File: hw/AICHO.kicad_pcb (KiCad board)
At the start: 2 copper layers, 100 x 58 mm, 77 parts, among them J1 Conn_01x06, J101 Conn_01x03, J102 Conn_01x02, J103 Conn_01x02, J104 Conn_01x02, J201 Conn_01x03, J202 Conn_01x02, J203 Conn_01x02, J204 Conn_01x02, J21 Conn_01x02, J22 Conn_01x02, J3 USB_A, J301 Conn_01x03, J302 Conn_01x02, J303 Conn_01x02, J304 Conn_01x02, J4 AudioJack3_SwitchTR, J401 Conn_01x03, J402 Conn_01x02, J403 Conn_01x02, J404 Conn_01x02, J5 Speaker, Q1 Si2302, Q10 Si2302, Q11 Si2302, Q12 Si2302, Q2 Si2302, Q3 Si2302, Q4 Si2302, Q5 Si2302, Q6 Si2302, Q7 Si2302, Q8 Si2302, Q9 Si2302, U1 RP2040, U2 W25Q128JVPIQ, U3 SPX3819M5-L-3-3, U4 USBLC6-2SC6, U5 MAX98357AETE+, Y1 12MHz

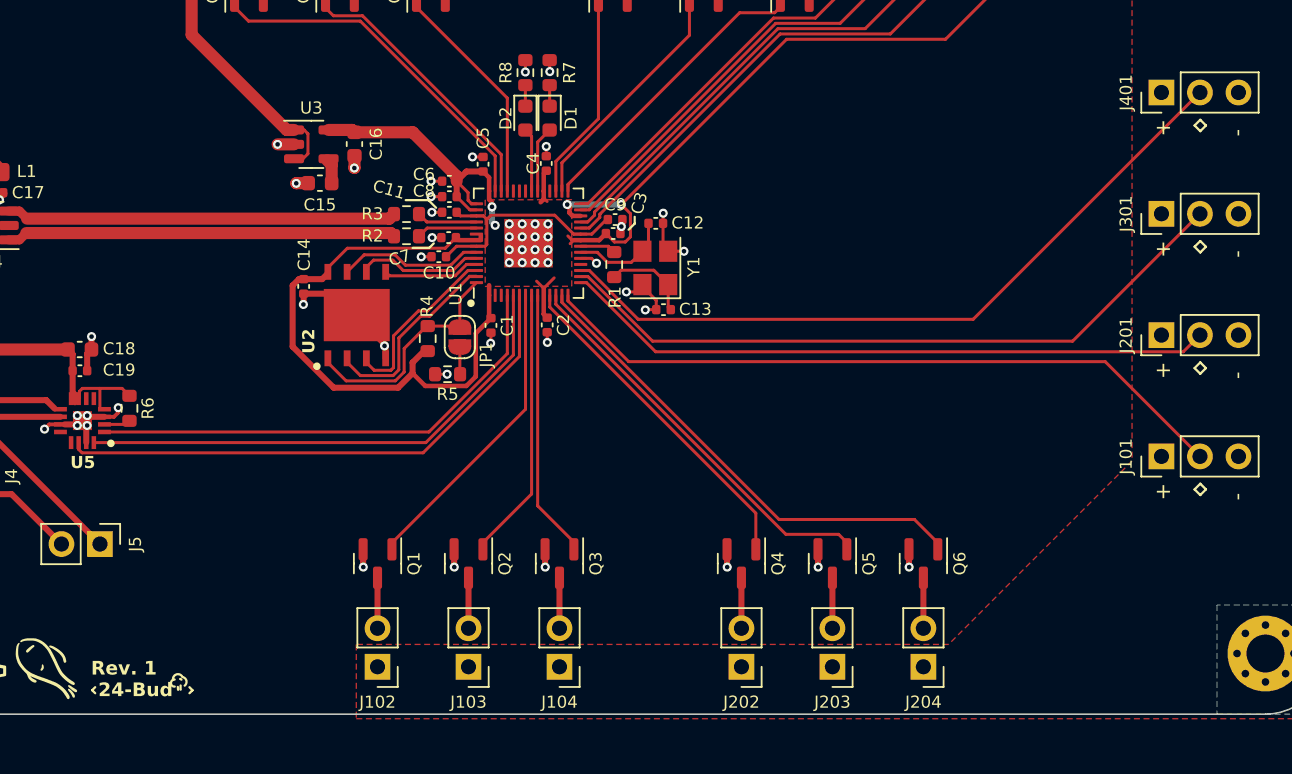
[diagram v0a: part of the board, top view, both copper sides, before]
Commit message: Fix missing level shifter and resubmit for fab >-<
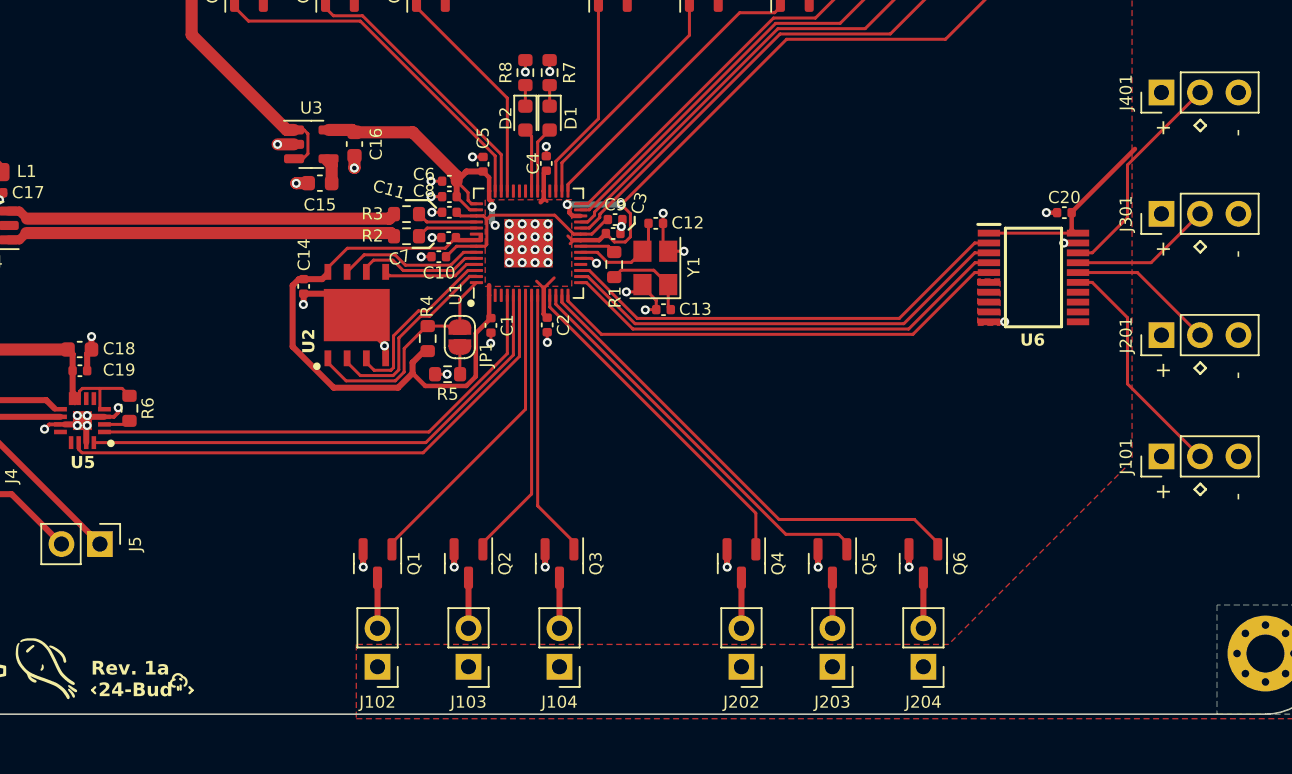
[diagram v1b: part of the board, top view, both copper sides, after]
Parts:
- added C20: 100n, Capacitor_SMD:C_0402_1005Metric, F.Cu at (112.7, 54.9)
- added U6: SN74AHCT245PWR, SN74AHCT245PWR:SOP65P640X120-20N, F.Cu at (110.7, 59.2)
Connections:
- J101 pad 2: /ORG1_LED -> /ORG1_LED_OUT
- J201 pad 2: /ORG2_LED -> /ORG2_LED_OUT
- J301 pad 2: /ORG3_LED -> /ORG3_LED_OUT
- J401 pad 2: /ORG4_LED -> /ORG4_LED_OUT
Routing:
- net /ORG4_LED: track 48.4 -> 30.3 mm
- net /ORG3_LED: track 46.1 -> 30.1 mm
- net /ORG1_LED: track 46.3 -> 30.7 mm
- net /ORG1_LED_OUT: track 0.00 -> 15.4 mm
- net /ORG4_LED_OUT: track 0.00 -> 14.5 mm
- net +5V: track 96.3 -> 109.8 mm
- net /ORG2_LED: track 43.2 -> 30.0 mm
- net /ORG2_LED_OUT: track 0.00 -> 9.75 mm
- net /ORG3_LED_OUT: track 0.00 -> 9.38 mm
- net GND: track 54.7 -> 57.4 mm, vias 62 -> 65
- added copper zone on F.Cu, net GND
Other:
- board text added: "Rev. 1a"
- board text removed: "Rev. 1"

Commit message: 🚧 Update layout
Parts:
- removed the R6 at (51.1, 67.8)
- added C20: 10u, Capacitor_SMD:C_0603_1608Metric, F.Cu at (57.3, 75.4)
- added C21: 100n, Capacitor_SMD:C_0402_1005Metric, F.Cu at (58.5, 74.8)
- added C22: 10u, Capacitor_SMD:C_0603_1608Metric, F.Cu at (57.2, 69.3)
- added C23: 100n, Capacitor_SMD:C_0402_1005Metric, F.Cu at (58.4, 69.9)
- added C24: 10u, Capacitor_SMD:C_0603_1608Metric, F.Cu at (69.9, 70.2)
- added C25: 100n, Capacitor_SMD:C_0402_1005Metric, F.Cu at (68.5, 70.4)
- added C26: 2.2u, Capacitor_SMD:C_0402_1005Metric, F.Cu at (61.7, 68.2)
- added C27: 2.2u, Capacitor_SMD:C_0402_1005Metric, F.Cu at (58.0, 71.5)
- added C28: 2.2n, Capacitor_SMD:C_0402_1005Metric, F.Cu at (56.0, 72.0)
- added C29: 2.2n, Capacitor_SMD:C_0402_1005Metric, F.Cu at (56.0, 73.8)
- added C30: 100n, Capacitor_SMD:C_0402_1005Metric, F.Cu at (54.5, 73.0)
- added C31: 1u, Capacitor_SMD:C_0402_1005Metric, F.Cu at (2.07, 97.9)
- added C32: 2.2u, Capacitor_SMD:C_0402_1005Metric, F.Cu at (2.07, 96.9)
- added C33: 470n, Capacitor_SMD:C_0402_1005Metric, F.Cu at (8.18, 97.3)
- added C34: 470n, Capacitor_SMD:C_0402_1005Metric, F.Cu at (4.04, 95.2)
- added C35: 100n, Capacitor_SMD:C_0402_1005Metric, F.Cu at (8.18, 98.8)
- added C36: 10u, Capacitor_SMD:C_0603_1608Metric, F.Cu at (-10.8, 101.1)
- added C37: 100n, Capacitor_SMD:C_0402_1005Metric, F.Cu at (-9.55, 101.1)
- added C38: 10u, Capacitor_SMD:C_0603_1608Metric, F.Cu at (-10.8, 98.1)
- added C39: 100n, Capacitor_SMD:C_0402_1005Metric, F.Cu at (-9.55, 99.3)
- added C40: 10u, Capacitor_SMD:C_0603_1608Metric, F.Cu at (-8.13, 95.5)
- added C41: 100n, Capacitor_SMD:C_0402_1005Metric, F.Cu at (-8.13, 96.7)
- added C42: 2.2u, Capacitor_SMD:C_0402_1005Metric, F.Cu at (2.05, 98.8)
- added C43: 2.2n, Capacitor_SMD:C_0402_1005Metric, F.Cu at (-0.29, 100.2)
- added J6: AudioJack3_SwitchTR, Connector_Audio:Jack_3.5mm_CUI_SJ1-3525N_Horizontal, F.Cu at (56.0, 93.5)
- added R10: 2.2k, Resistor_SMD:R_0402_1005Metric, F.Cu at (9.58, 98.4)
- added R11: 150k, Resistor_SMD:R_0402_1005Metric, F.Cu at (7.25, 95.2)
- added R12: 100k, Resistor_SMD:R_0402_1005Metric, F.Cu at (8.19, 96.4)
- added R13: 470, Resistor_SMD:R_0402_1005Metric, F.Cu at (0.20, 98.8)
- added R8: 470, Resistor_SMD:R_0402_1005Metric, F.Cu at (58.0, 72.4)
- added R9: 470, Resistor_SMD:R_0402_1005Metric, F.Cu at (58.0, 73.3)
- added U6: OPA1622, Package_SON:Texas_S-PVSON-N10, F.Cu at (51.8, 73.0)
- added U7: MAX9814, Package_DFN_QFN:DFN-14-1EP_3x3mm_P0.4mm_EP1.78x2.35mm, F.Cu at (5.13, 97.5)
- added U8: PCM1808PWR, PCM1808PWR:PCM1808PWR, F.Cu at (-4.95, 100.5)
- U5: value MAX98357AETE+ -> PCM5102A; footprint MAX98357AETE+:QFN50P300X300X80-17N -> Package_SO:TSSOP-20_4.4x6.5mm_P0.65mm
- moved C18 21.1 mm to (68.5, 67.9)
- moved C19 20.2 mm to (67.5, 69.7), turned to -90 degrees
- moved U5 15.3 mm to (62.9, 72.3), turned to 0 degrees
- moved G*** 10.0 mm to (45.7, 95.1)
- moved G*** 10.0 mm to (40.7, 94.9)
- moved H2 10.0 mm to (34.0, 94.0)
- moved H3 10.0 mm to (126.0, 94.0)
- moved J102 10.0 mm to (67.4, 94.9)
- moved J103 10.0 mm to (73.4, 94.9)
- moved J104 10.0 mm to (79.4, 94.9)
- moved J202 10.0 mm to (91.4, 94.9)
- moved J203 10.0 mm to (97.4, 94.9)
- moved J204 10.0 mm to (103.4, 94.9)
- moved J4 10.0 mm to (34.5, 82.3)
- moved Q1 10.0 mm to (67.4, 88.1)
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- renumbered C20 to C45, J3 to J2, R7 to R6, R8 to R7, U6 to U9
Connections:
- C18 pad 1: +5V -> +3V3
- C19 pad 1: +5V -> +3V3
- J4 pad R: /AUDIO_OUT+ -> /AUDIO_OUT_R
- J4 pad RN: /AUDIO_SPEAKER+ -> unconnected-(J4-PadRN)
- J4 pad S: /AUDIO_OUT- -> GND
- J4 pad T: /AUDIO_OUT+ -> /AUDIO_OUT_L
- J4 pad TN: unconnected-(J4-PadTN) -> /AUDIO_SPEAKER+
- J5 pad 2: /AUDIO_OUT- -> GND
- U1 pad 11: /ORG2_SOLENOID -> /MIC_SHDN
- U1 pad 12: /ORG2_PUMP_INFLATE -> unconnected-(U1-GPIO9-Pad12)
- U1 pad 13: /ORG2_PUMP_DRAIN -> /ORG1_SOLENOID
- U1 pad 14: /ORG1_LED -> /ORG1_PUMP_INFLATE
- U1 pad 15: /ORG2_LED -> /ORG1_PUMP_DRAIN
- U1 pad 16: /ORG3_LED -> /ORG2_SOLENOID
- U1 pad 17: /ORG4_LED -> /ORG2_PUMP_INFLATE
- U1 pad 18: unconnected-(U1-GPIO15-Pad18) -> /ORG2_PUMP_DRAIN
- U1 pad 29: /ORG3_SOLENOID -> /ORG1_LED
- U1 pad 3: unconnected-(U1-GPIO1-Pad3) -> /I2S_SD
- U1 pad 30: /ORG3_PUMP_INFLATE -> /ORG2_LED
- U1 pad 31: /ORG3_PUMP_DRAIN -> /ORG3_LED
- U1 pad 32: unconnected-(U1-GPIO21-Pad32) -> /ORG4_LED
- U1 pad 34: /ACT1 -> /ORG3_SOLENOID
- U1 pad 35: /ACT2 -> /ORG3_PUMP_INFLATE
- U1 pad 36: unconnected-(U1-GPIO24-Pad36) -> /ORG3_PUMP_DRAIN
- U1 pad 37: unconnected-(U1-GPIO25-Pad37) -> /ACT1
- U1 pad 38: unconnected-(U1-GPIO26_ADC0-Pad38) -> /ACT2
- U1 pad 4: /I2S_SD -> /I2S_CK
- U1 pad 5: /I2S_CK -> /I2S_WS
- U1 pad 6: /I2S_WS -> /MIC_ADC_SD
- U1 pad 7: /ORG1_SOLENOID -> /MIC_ADC_CK
- U1 pad 8: /ORG1_PUMP_INFLATE -> /MIC_ADC_WS
- U1 pad 9: /ORG1_PUMP_DRAIN -> /MIC_ADC_SCK
- U5 pad 1: /I2S_SD -> +3V3
- U5 pad 10: /AUDIO_OUT- -> GND
- U5 pad 13: unconnected-(U5-N.C._4-Pad13) -> /I2S_CK
- U5 pad 14: /I2S_WS -> /I2S_SD
- U5 pad 15: GND -> /I2S_WS
- U5 pad 16: /I2S_CK -> GND
- U5 pad 17: GND -> +3V3
- U5 pad 4: +5V -> Net-(U5-CAPM)
- U5 pad 5: unconnected-(U5-N.C._1-Pad5) -> Net-(U5-VNEG)
- U5 pad 6: unconnected-(U5-N.C._2-Pad6) -> Net-(U5-OUTL)
- U5 pad 7: +5V -> Net-(U5-OUTR)
- U5 pad 8: +5V -> +3V3
- U5 pad 9: /AUDIO_OUT+ -> GND
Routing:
- net /I2S_CK: track 34.0 -> 3.84 mm
- net /ORG1_LED: track 30.7 -> 0.94 mm
- net /ORG4_LED: track 30.3 -> 0.94 mm
- net /ORG3_LED: track 30.1 -> 0.94 mm
- net /I2S_WS: track 36.3 -> 7.08 mm
- net /ORG2_LED: track 30.0 -> 0.92 mm
- net /AUDIO_OUT-: track 28.1 -> 0.00 mm
- net /I2S_SD: track 32.6 -> 7.99 mm
- net /AUDIO_OUT+: track 24.4 -> 0.00 mm
- net /ORG2_PUMP_INFLATE: track 26.7 -> 5.26 mm
- net /ORG2_PUMP_DRAIN: track 32.2 -> 11.5 mm
- net /ORG3_SOLENOID: track 19.7 -> 0.00 mm
- net /ORG2_SOLENOID: track 22.4 -> 2.86 mm
- net /ORG1_SOLENOID: track 20.4 -> 0.89 mm
- net /ORG3_PUMP_INFLATE: track 16.0 -> 0.00 mm
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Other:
- board size 100 x 58 mm -> 100 x 68 mm

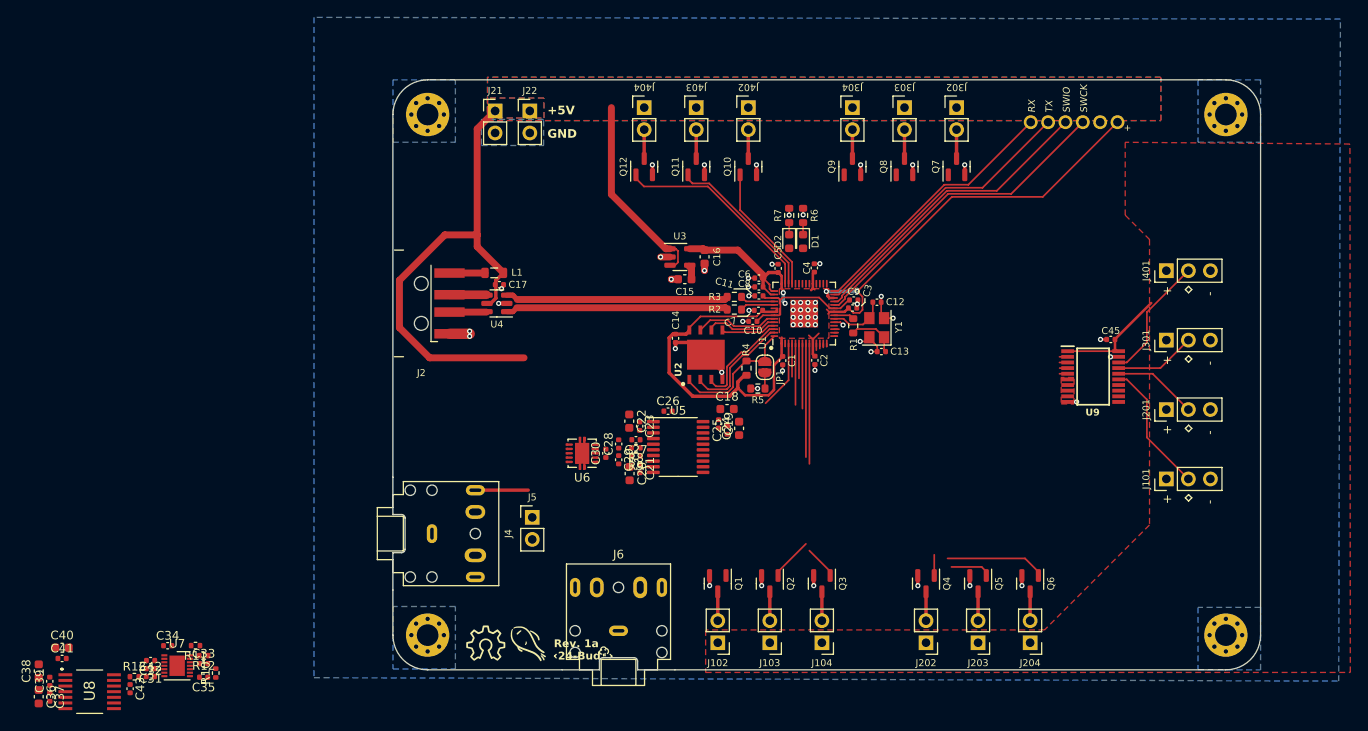
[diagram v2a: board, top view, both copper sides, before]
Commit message: Finish updated board layout & routing
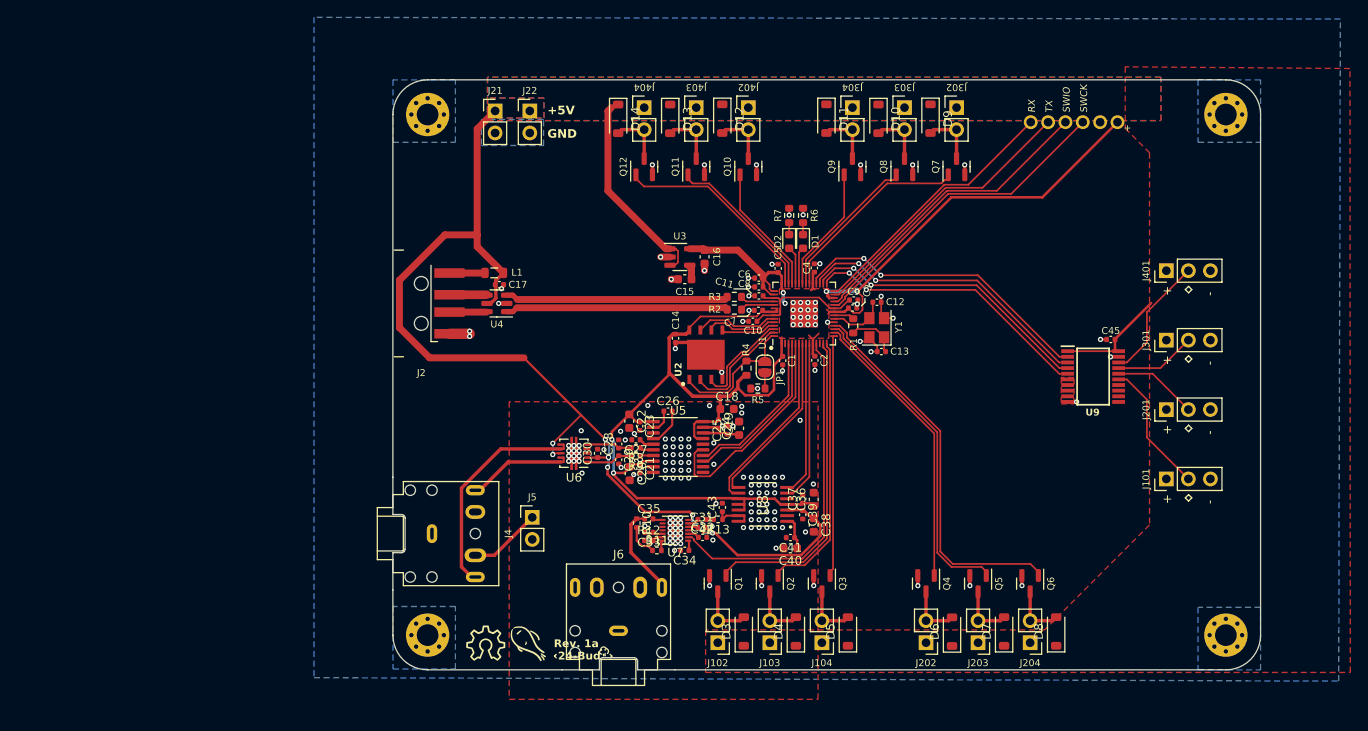
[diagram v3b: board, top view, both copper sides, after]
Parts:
- added D10: MBR0530, Diode_SMD:D_SOD-123, F.Cu at (86.0, 34.5)
- added D11: MBR0530, Diode_SMD:D_SOD-123, F.Cu at (80.0, 34.5)
- added D12: MBR0530, Diode_SMD:D_SOD-123, F.Cu at (68.0, 34.5)
- added D13: MBR0530, Diode_SMD:D_SOD-123, F.Cu at (62.0, 34.5)
- added D14: MBR0530, Diode_SMD:D_SOD-123, F.Cu at (56.0, 34.5)
- added D3: MBR0530, Diode_SMD:D_SOD-123, F.Cu at (70.4, 93.6)
- added D4: MBR0530, Diode_SMD:D_SOD-123, F.Cu at (76.4, 93.6)
- added D5: MBR0530, Diode_SMD:D_SOD-123, F.Cu at (82.4, 93.6)
- added D6: MBR0530, Diode_SMD:D_SOD-123, F.Cu at (94.4, 93.6)
- added D7: MBR0530, Diode_SMD:D_SOD-123, F.Cu at (100.4, 93.6)
- added D8: MBR0530, Diode_SMD:D_SOD-123, F.Cu at (106.4, 93.6)
- added D9: MBR0530, Diode_SMD:D_SOD-123, F.Cu at (92.0, 34.5)
- moved C36 92.2 mm to (78.5, 78.3), turned to 90 degrees
- moved C38 90.9 mm to (78.5, 81.3), turned to -90 degrees
- moved C37 89.7 mm to (77.2, 78.3), turned to 90 degrees
- moved C39 88.9 mm to (77.2, 80.1), turned to -90 degrees
- moved C41 85.1 mm to (75.8, 82.8), turned to 180 degrees
- moved C40 84.7 mm to (75.8, 84.0), turned to 180 degrees
- moved U8 80.5 mm to (72.6, 78.9), turned to 90 degrees
- moved C43 71.4 mm to (68.0, 79.3), turned to 90 degrees
- moved R13 69.7 mm to (67.5, 80.7), turned to 180 degrees
- moved C42 66.1 mm to (65.6, 80.7), turned to 180 degrees
- moved C31 65.6 mm to (65.6, 81.6), turned to 0 degrees
- moved C32 65.2 mm to (65.7, 82.7), turned to 0 degrees
- moved C34 60.6 mm to (63.6, 84.2), turned to 180 degrees
- moved U7 59.5 mm to (62.5, 81.9), turned to 180 degrees
- moved C35 54.5 mm to (59.5, 80.6), turned to 0 degrees
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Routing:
- net +5V: track 93.9 -> 159.7 mm, vias 0 -> 8
- net +3V3: track 119.5 -> 176.8 mm, vias 4 -> 6
- net /MIC_SHDN: track 0.78 -> 40.5 mm
- net /ORG1_SOLENOID: track 0.89 -> 36.7 mm
- net /ORG4_LED: track 0.94 -> 35.3 mm, vias 0 -> 2
- net /ORG3_LED: track 0.94 -> 34.6 mm, vias 0 -> 2
- net /ORG2_LED: track 0.92 -> 33.9 mm, vias 0 -> 2
- net /ORG2_PUMP_INFLATE: track 5.26 -> 38.0 mm
- net /ORG2_PUMP_DRAIN: track 11.5 -> 44.2 mm
- net /ORG1_LED: track 0.94 -> 33.3 mm, vias 0 -> 2
- net /ORG2_SOLENOID: track 2.86 -> 33.1 mm
- net /ORG1_PUMP_INFLATE: track 5.35 -> 30.7 mm
- net /AUDIO_OUT_L: track 0.00 -> 25.0 mm
- net /ORG1_PUMP_DRAIN: track 4.24 -> 28.2 mm
- net /ORG3_SOLENOID: track 0.00 -> 22.4 mm
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
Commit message: Yes, this is
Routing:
- net +5V: track 159.7 -> 158.8 mm, vias 8 -> 7
- net GND: vias 169 -> 182
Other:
- board text added: "24-Awn"
- board text added: "Headphone Out"
- board text added: "Mic In"
- board text added: "Rev. 2"
- board text removed: "24-Bud"
- board text removed: "Rev. 1a"
